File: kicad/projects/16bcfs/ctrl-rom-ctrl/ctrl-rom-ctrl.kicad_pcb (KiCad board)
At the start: 4 copper layers, 88.9 x 43.2 mm, 68 parts, among them J1 Instruction, J2 Control ROM Address, J3 Raw Address for Pgm ROM, J4 Signal Header, J5 Power, J6 Power, U1 74HC08, U11 74HC157, U12 74HC157, U13 74HC157, U14 74HC157, U15 74HC193, U16 74HC193, U17 74HC193, U18 74HC193, U19 74HC04, U2 74HC74, U21 74HC08, U22 74HC08, U23 74HC32, U3 74HC03, U4 74HC193, U6 74HC00, U7 74HC00, U9 74HC165, X1 XO32

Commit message: Rename #RHLD to #CPYHLD on the Ctrl Rom Ctrl & Midplane
The logic for the signal does not change, but the purpose does.  The
Reset Circuit will handle the #RHLD now, but it needs to know when the
copy is complete.
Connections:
- net ~{RHLD} renamed ~{CPYHLD}
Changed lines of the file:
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@@
   (net 48 "PGM_AE")
   (net 49 "~{RESET}")
-  (net 50 "~{RHLD}")
+  (net 50 "~{CPYHLD}")
   (net 51 "~{QR}")
   (net 52 "~{DONE}")
@@
       (net 49 "~{RESET}") (pinfunction "Pin_1") (pintype "passive"))
     (pad "2" thru_hole oval (at 0 -2.54 270) (size 1.7 1.7) (drill 1) (layers "*.Cu" "*.Mask")
-      (net 50 "~{RHLD}") (pinfunction "Pin_2") (pintype "passive"))
+      (net 50 "~{CPYHLD}") (pinfunction "Pin_2") (pintype "passive"))
     (pad "3" thru_hole oval (at 0 -5.08 270) (size 1.7 1.7) (drill 1) (layers "*.Cu" "*.Mask")
       (net 51 "~{QR}") (pinfunction "Pin_3") (pintype "passive"))
@@
       (net 52 "~{DONE}") (pintype "input"))
     (pad "3" smd roundrect (at -2.475 1.27 180) (size 1.95 0.6) (layers "B.Cu" "B.Paste" "B.Mask") (roundrect_rratio 0.25)
-      (net 50 "~{RHLD}") (pintype "output"))
+      (net 50 "~{CPYHLD}") (pintype "output"))
     (pad "4" smd roundrect (at -2.475 0 180) (size 1.95 0.6) (layers "B.Cu" "B.Paste" "B.Mask") (roundrect_rratio 0.25)
       (net 74 "Net-(R16-Pad2)") (pintype "input"))
@@
     )
   )
-  (zone (net 50) (net_name "~{RHLD}") (layer "B.Cu") (name "$teardrop_padvia$") (hatch edge 0.5)
+  (zone (net 50) (net_name "~{CPYHLD}") (layer "B.Cu") (name "$teardrop_padvia$") (hatch edge 0.5)
     (priority 30017)
     (attr (teardrop (type padvia)))
@@
     )
   )
-  (zone (net 50) (net_name "~{RHLD}") (layer "B.Cu") (name "$teardrop_padvia$") (hatch edge 0.5)
+  (zone (net 50) (net_name "~{CPYHLD}") (layer "B.Cu") (name "$teardrop_padvia$") (hatch edge 0.5)
     (priority 30077)
     (attr (teardrop (type padvia)))

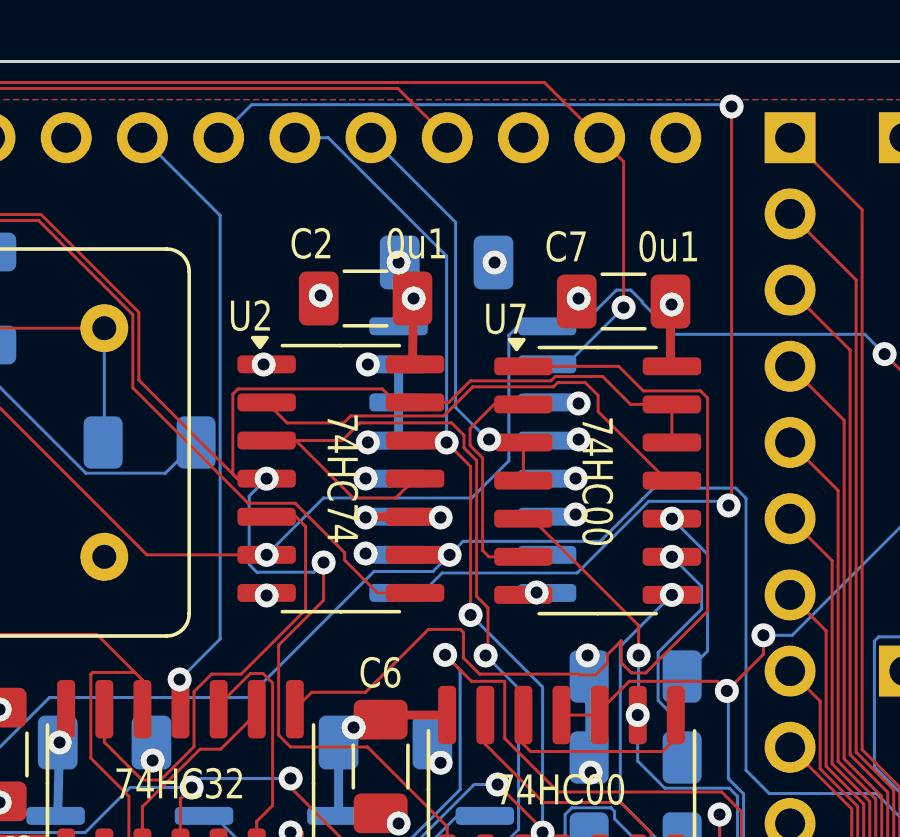
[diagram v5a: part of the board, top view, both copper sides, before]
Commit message: Look at the MAX704 uProcessor Supervisor
This commit adds the documentation for the MAX704 supervisor.  Some
minor update in teh Control Rom Control circuit are added as well.

Closes #198
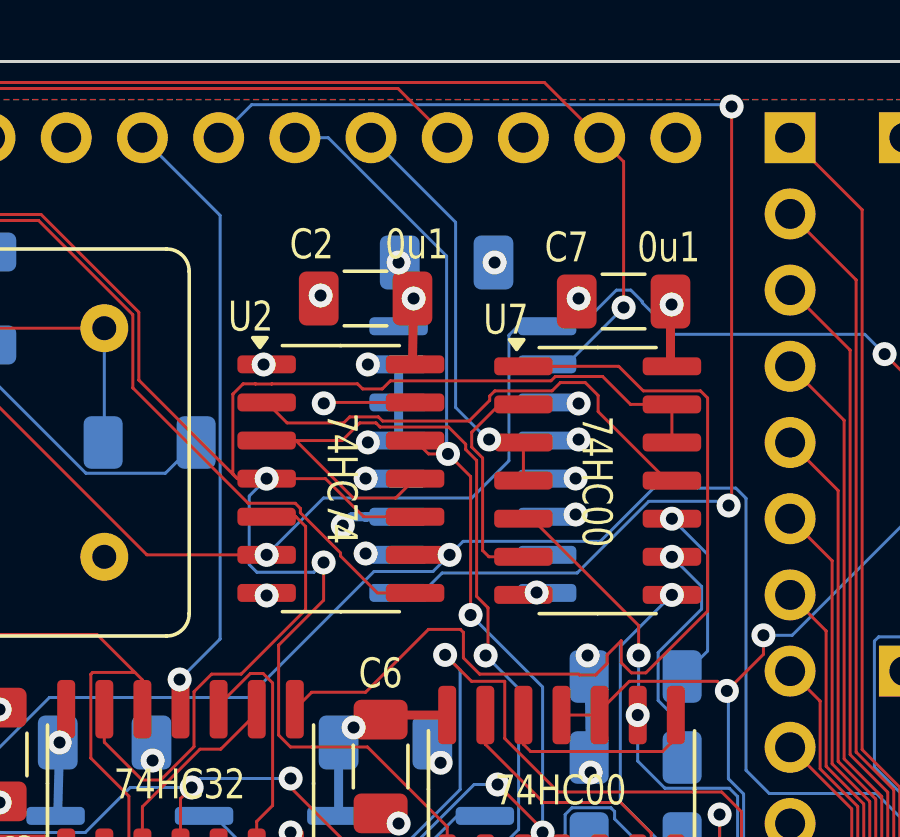
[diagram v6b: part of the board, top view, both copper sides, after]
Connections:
- U2 pad 10: VCC -> ~{RESET}
- U2 pad 13: ~{RESET} -> VCC
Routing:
- net ~{RESET}: track 71.1 -> 77.0 mm
- net VCC: track 316.7 -> 320.1 mm
- net ~{QL}: track 7.80 -> 6.85 mm
- net QC: track 64.5 -> 65.4 mm
